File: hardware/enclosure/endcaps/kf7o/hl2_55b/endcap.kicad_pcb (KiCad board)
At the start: 2 copper layers, 106 x 55 mm, 14 parts, among them Q1 DTC144E, Q2 IRLML6402

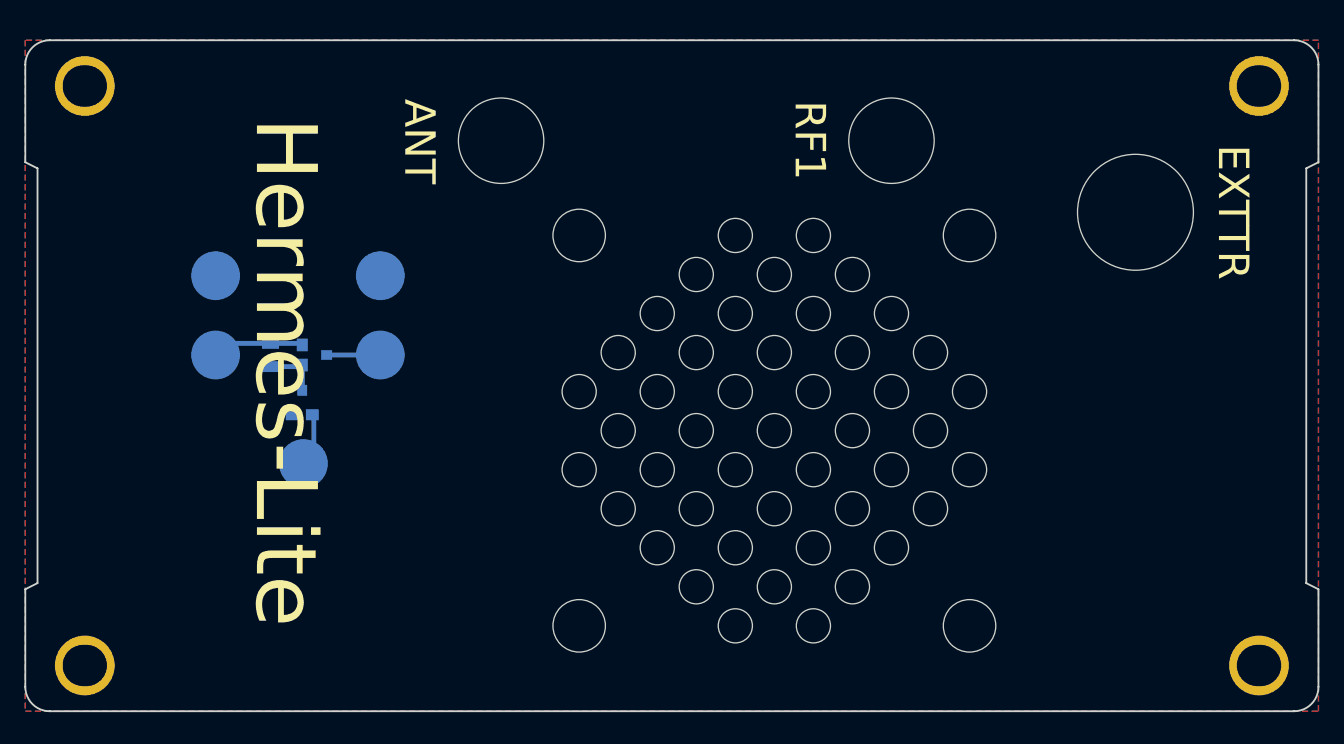
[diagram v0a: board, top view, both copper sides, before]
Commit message: 55mm rev2 endplate
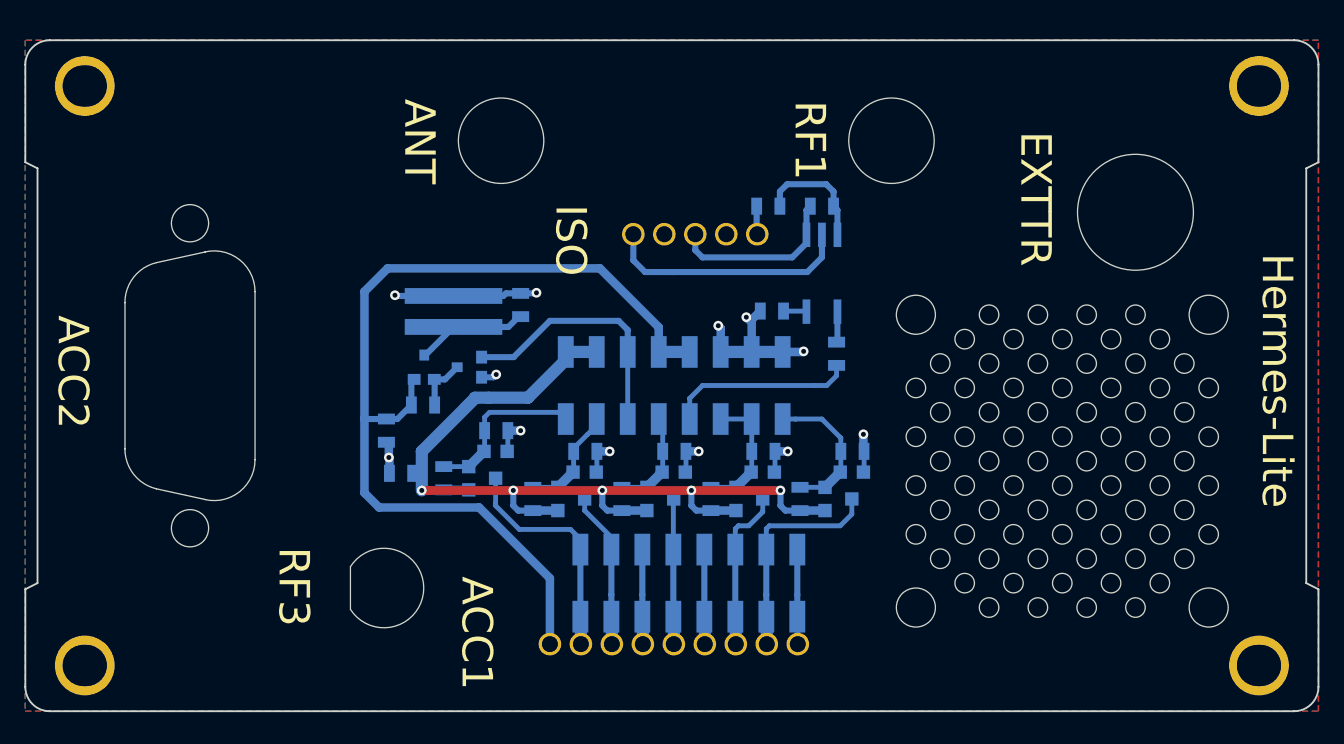
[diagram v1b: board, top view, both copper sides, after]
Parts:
- removed the REF** at (95.4, 66.0)
- removed TP1: Power, TestPoint:TestPoint_Pad_D4.0mm
- removed TP2: Fan Control, TestPoint:TestPoint_Pad_D4.0mm
- removed TP3, TP5: Ground, TestPoint:TestPoint_Pad_D4.0mm
- removed TP4: Fan Power, TestPoint:TestPoint_Pad_D4.0mm
- added ACC1: Terminal Block, endcaplib:terminal_block, B.Cu at (93.0, 99.5)
- added ACC2: DB9, endcaplib:db9inside, B.Cu at (63.5, 77.5)
- added C1: 0.1uF, endcaplib:SMD-0805, B.Cu at (115.3, 63.6)
- added C2: 0.1uF, endcaplib:SMD-0805, B.Cu at (79.6, 82.0)
- added C3: 0.1uF, endcaplib:SMD-0805, B.Cu at (80.8, 85.5)
- added C4: 0.1uF, endcaplib:SMD-0805, B.Cu at (90.6, 71.7)
- added FB1: Ferrite_Bead_Small, endcaplib:SMD-0805, B.Cu at (110.9, 63.6)
- added ISO1: Terminal Block, endcaplib:terminal_block5, B.Cu at (110.0, 65.9)
- added J2: Male Header, endcaplib:male_header, B.Cu at (94.3, 78.3)
- added J3: Male Header, endcaplib:male_header, B.Cu at (95.5, 94.5)
- added J4: Fan, endcaplib:male_header_2, B.Cu at (85.1, 73.5)
- added Q3: MULTIFET, endcaplib:3sot3_3, B.Cu at (89.5, 83.7)
- added Q4: MULTIFET, endcaplib:3sot3_3, B.Cu at (96.8, 85.4)
- added Q5: MULTIFET, endcaplib:3sot3_3, B.Cu at (104.1, 85.4)
- added Q6: MULTIFET, endcaplib:3sot3_3, B.Cu at (111.4, 85.4)
- added Q7: MULTIFET, endcaplib:3sot3_3, B.Cu at (118.7, 85.4)
- added R10: 10K, endcaplib:SMD-0805, B.Cu at (113.5, 87.6)
- added R11: 10K, endcaplib:SMD-0805, B.Cu at (117.8, 83.7)
- added R12: 1K, endcaplib:SMD-0805, B.Cu at (116.5, 75.7)
- added R13: 680, endcaplib:SMD-0805, B.Cu at (111.2, 72.2)
- added R2: 10K, endcaplib:SMD-0805, B.Cu at (84.3, 85.9)
- added R3: 10K, endcaplib:SMD-0805, B.Cu at (88.6, 82.0)
- added R4: 10K, endcaplib:SMD-0805, B.Cu at (91.6, 87.6)
- added R5: 10K, endcaplib:SMD-0805, B.Cu at (95.9, 83.7)
- added R6: 10K, endcaplib:SMD-0805, B.Cu at (98.9, 87.6)
- added R7: 10K, endcaplib:SMD-0805, B.Cu at (103.2, 83.7)
- added R8: 10K, endcaplib:SMD-0805, B.Cu at (106.2, 87.6)
- added R9: 10K, endcaplib:SMD-0805, B.Cu at (110.5, 83.7)
- added REF**: fan30, endcaplib:fan30, B.Cu at (123.0, 72.5)
- added RF3: SMA, endcaplib:sma_panel, B.Cu at (79.4, 94.9)
- added U1: ACPL-M21L-000E, Package_SO:SO-5_4.4x3.6mm_P1.27mm, B.Cu at (115.3, 69.1)
- moved Q1 15.2 mm to (87.4, 76.8), turned to 270 degrees
- moved R1 13.2 mm to (82.6, 79.9), turned to 0 degrees
- moved Q2 10.2 mm to (82.7, 77.8), turned to 180 degrees
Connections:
- net Earth renamed GNDS
- net Net-(Q2-Pad2) renamed VSUP
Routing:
- net Vlvds: track 0.00 -> 76.6 mm, vias 0 -> 5
- net VSUP: track 7.50 -> 78.0 mm
- net GNDS: track 0.00 -> 50.9 mm, vias 0 -> 12
- net Net-(ISO1-Pad5): track 0.00 -> 20.5 mm
- net Net-(ACC1-Pad2): track 0.00 -> 19.0 mm
- net Net-(ACC1-Pad8): track 0.00 -> 18.2 mm
- net Net-(J2-Pad5): track 4.35 -> 21.5 mm
- net ISOIN: track 0.00 -> 15.4 mm
- net Net-(J2-Pad2): track 0.00 -> 14.9 mm
- net Net-(C1-Pad2): track 0.00 -> 14.3 mm
- net Net-(J2-Pad16): track 0.00 -> 14.2 mm
- net Net-(ACC1-Pad7): track 0.00 -> 13.3 mm
- net Net-(ACC1-Pad3): track 0.00 -> 12.8 mm
- net Net-(ACC1-Pad5): track 0.00 -> 11.9 mm
- net Net-(J2-Pad12): track 0.00 -> 11.9 mm
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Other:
- board text added: "ACC1"
- board text added: "ACC2"
- board text added: "ISO"
- board text added: "RF3"

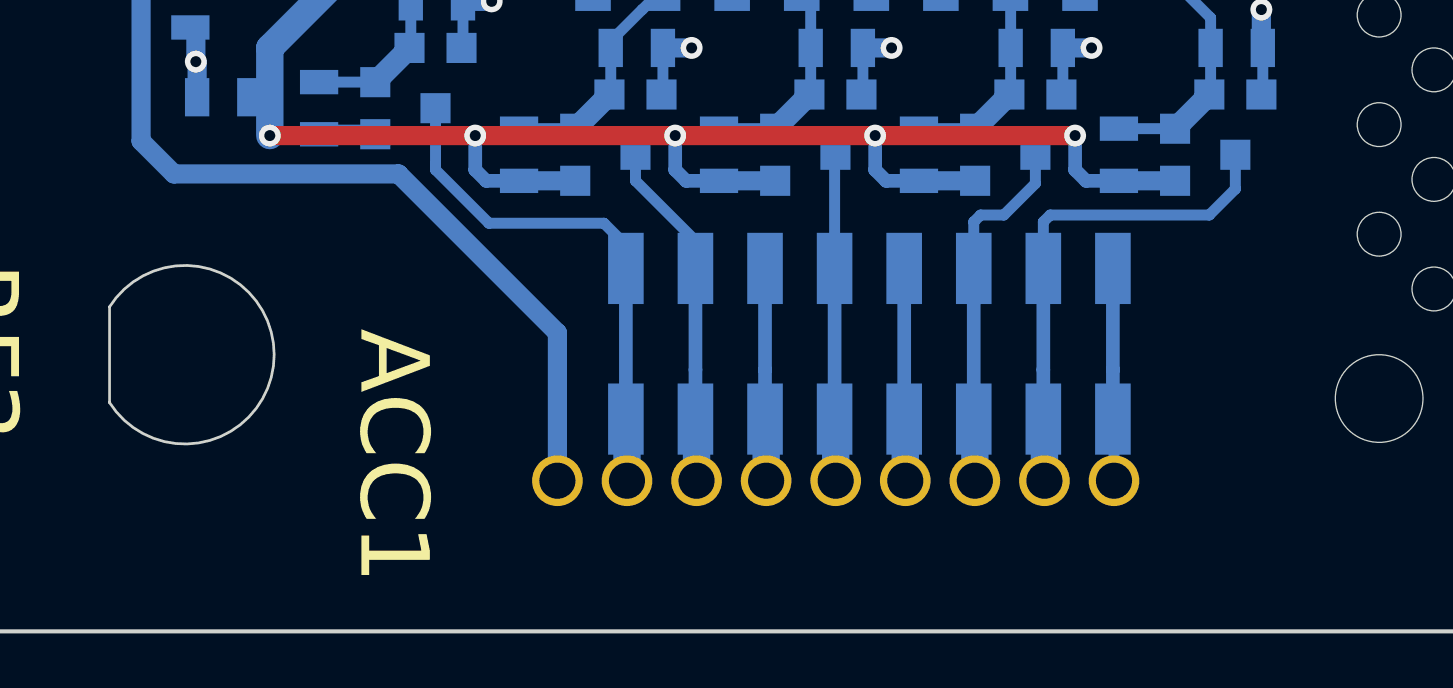
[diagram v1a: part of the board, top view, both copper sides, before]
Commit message: Added pullups, diodes to some channels
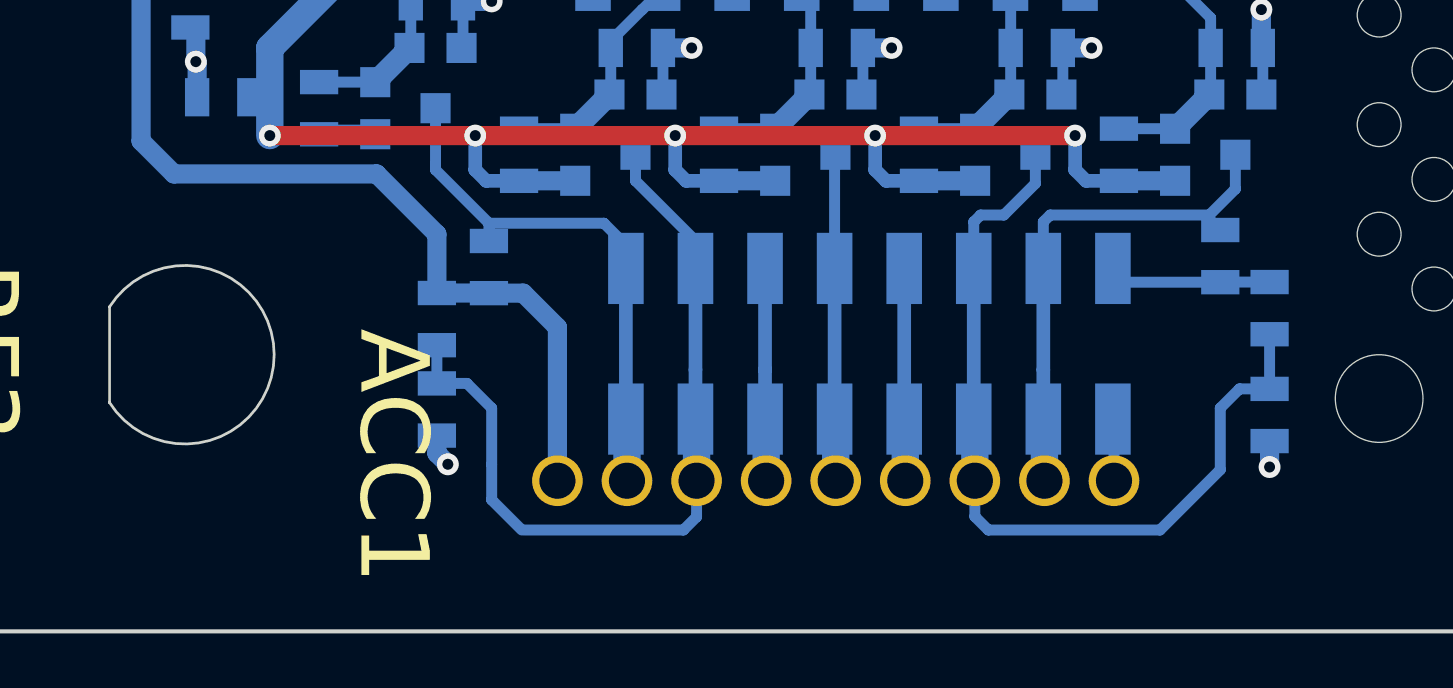
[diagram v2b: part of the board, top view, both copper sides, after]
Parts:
- added D1: 1N4148, endcaplib:SMD-0805, B.Cu at (119.0, 97.1)
- added D2: 1N4148, endcaplib:SMD-0805, B.Cu at (88.6, 96.9)
- added R14: 10K, endcaplib:SMD-0805, B.Cu at (117.2, 91.3)
- added R15: 10K, endcaplib:SMD-0805, B.Cu at (119.0, 93.2)
- added R16: 10K, endcaplib:SMD-0805, B.Cu at (88.6, 93.6)
- added R17: 10K, endcaplib:SMD-0805, B.Cu at (90.5, 91.7)
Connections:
- J3 pad 15: GNDS -> Net-(J3-Pad15)
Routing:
- net Net-(ACC1-Pad7): track 13.3 -> 31.1 mm
- net Net-(ACC1-Pad3): track 12.8 -> 29.3 mm
- net Net-(J3-Pad15): track 0.00 -> 5.93 mm
- net GNDS: track 50.9 -> 47.5 mm, vias 12 -> 14
- net VSUP: track 78.0 -> 79.4 mm
- net Net-(ACC1-Pad8): track 18.2 -> 18.9 mm
- net Net-(ACC1-Pad2): track 19.0 -> 19.6 mm

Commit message: Final IO end plates
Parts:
- added G***: OSHW-logo_silkscreen-back_2mm, HERMESLITE:OSHW-logo_silkscreen-back_2mm, B.Cu at (126.3, 53.6)
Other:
- board text added: "HL2 IO End Plate v2.0 © 2019 SofterHardware"
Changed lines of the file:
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@@
   (general
     (thickness 1.6)
-    (drawings 32)
+    (drawings 33)
     (tracks 288)
     (zones 0)
-    (modules 45)
+    (modules 46)
     (nets 29)
   )
@@
   (title_block
     (title "Hermes-Lite End Plate 55")
-    (date 2019-11-24)
+    (date 2019-12-01)
     (rev 2.0)
     (company SofterHardware)
@@
   )
   (setup
-    (last_trace_width 0.4)
+    (last_trace_width 0.25)
     (user_trace_width 0.2)
     (user_trace_width 0.4)
@@
     )
   )
+  (module HERMESLITE:OSHW-logo_silkscreen-back_2mm (layer B.Cu)
+    (at 126.3 53.6 180)
+    (fp_text reference G*** (at 0 -1.05918 180) (layer B.SilkS) hide
+      (effects (font (size 0.0889 0.0889) (thickness 0.01778)) (justify mirror))
+    )
+    (fp_text value OSHW-logo_silkscreen-back_2mm (at 0 1.05918 180) (layer B.SilkS) hide
+      (effects (font (size 0.0889 0.0889) (thickness 0.01778)) (justify mirror))
+    )
+    (fp_poly (pts (xy 0.60452 -0.89662) (xy 0.59436 -0.89154) (xy 0.5715 -0.8763) (xy 0.53848 -0.85598)
+      (xy 0.49784 -0.82804) (xy 0.45974 -0.80264) (xy 0.42672 -0.77978) (xy 0.40386 -0.76454)
+      (xy 0.3937 -0.75946) (xy 0.38862 -0.762) (xy 0.37084 -0.77216) (xy 0.3429 -0.78486)
+      (xy 0.32766 -0.79248) (xy 0.30226 -0.80518) (xy 0.28956 -0.80772) (xy 0.28702 -0.80264)
+      (xy 0.27686 -0.78486) (xy 0.26416 -0.75184) (xy 0.24384 -0.70866) (xy 0.22352 -0.65786)
+      (xy 0.20066 -0.60198) (xy 0.1778 -0.5461) (xy 0.15494 -0.49276) (xy 0.13462 -0.4445)
+      (xy 0.11938 -0.4064) (xy 0.10922 -0.37846) (xy 0.10414 -0.3683) (xy 0.10668 -0.36576)
+      (xy 0.11938 -0.35306) (xy 0.1397 -0.33782) (xy 0.18796 -0.29718) (xy 0.23368 -0.23876)
+      (xy 0.26416 -0.17272) (xy 0.27178 -0.09906) (xy 0.26416 -0.03302) (xy 0.23876 0.03048)
+      (xy 0.19304 0.09144) (xy 0.13716 0.13462) (xy 0.07112 0.16256) (xy 0 0.17018)
+      (xy -0.06858 0.16256) (xy -0.13462 0.13716) (xy -0.19558 0.09144) (xy -0.21844 0.0635)
+      (xy -0.254 0.00254) (xy -0.27432 -0.05842) (xy -0.27432 -0.07366) (xy -0.27178 -0.14478)
+      (xy -0.25146 -0.21336) (xy -0.2159 -0.27178) (xy -0.16256 -0.32258) (xy -0.15748 -0.32766)
+      (xy -0.13208 -0.34544) (xy -0.11684 -0.3556) (xy -0.10414 -0.36576) (xy -0.19304 -0.58166)
+      (xy -0.20828 -0.61722) (xy -0.23368 -0.67564) (xy -0.254 -0.72644) (xy -0.27178 -0.76708)
+      (xy -0.28448 -0.79248) (xy -0.28956 -0.80518) (xy -0.29718 -0.80518) (xy -0.31242 -0.8001)
+      (xy -0.3429 -0.78486) (xy -0.36322 -0.7747) (xy -0.38608 -0.76454) (xy -0.39624 -0.75946)
+      (xy -0.4064 -0.76454) (xy -0.42672 -0.77978) (xy -0.45974 -0.8001) (xy -0.49784 -0.8255)
+      (xy -0.5334 -0.8509) (xy -0.56896 -0.87376) (xy -0.59182 -0.889) (xy -0.60452 -0.89662)
+      (xy -0.60706 -0.89662) (xy -0.61722 -0.889) (xy -0.63754 -0.87376) (xy -0.66548 -0.84582)
+      (xy -0.70612 -0.80518) (xy -0.71374 -0.8001) (xy -0.74676 -0.76454) (xy -0.7747 -0.73406)
+      (xy -0.79502 -0.71374) (xy -0.8001 -0.70612) (xy -0.79502 -0.69342) (xy -0.77978 -0.66802)
+      (xy -0.75692 -0.635) (xy -0.72898 -0.59436) (xy -0.65786 -0.49022) (xy -0.6985 -0.3937)
+      (xy -0.70866 -0.36322) (xy -0.7239 -0.32766) (xy -0.7366 -0.30226) (xy -0.74168 -0.28956)
+      (xy -0.75184 -0.28702) (xy -0.77978 -0.2794) (xy -0.81788 -0.27178) (xy -0.8636 -0.26416)
+      (xy -0.90932 -0.254) (xy -0.94742 -0.24638) (xy -0.9779 -0.2413) (xy -0.9906 -0.23876)
+      (xy -0.99314 -0.23622) (xy -0.99568 -0.23114) (xy -0.99822 -0.21844) (xy -0.99822 -0.19304)
+      (xy -0.99822 -0.15494) (xy -0.99822 -0.09906) (xy -0.99822 -0.09398) (xy -0.99822 -0.04064)
+      (xy -0.99822 0) (xy -0.99568 0.0254) (xy -0.99314 0.03556) (xy -0.98044 0.04064)
+      (xy -0.9525 0.04572) (xy -0.9144 0.05334) (xy -0.86614 0.0635) (xy -0.8636 0.0635)
+      (xy -0.81534 0.07112) (xy -0.77724 0.08128) (xy -0.7493 0.08636) (xy -0.7366 0.09144)
+      (xy -0.73406 0.09398) (xy -0.7239 0.11176) (xy -0.7112 0.14224) (xy -0.69596 0.1778)
+      (xy -0.68072 0.21336) (xy -0.66548 0.24892) (xy -0.65786 0.27178) (xy -0.65532 0.28448)
+      (xy -0.66294 0.29464) (xy -0.67818 0.32004) (xy -0.70104 0.35306) (xy -0.72898 0.3937)
+      (xy -0.73152 0.39878) (xy -0.75946 0.43688) (xy -0.77978 0.47244) (xy -0.79502 0.4953)
+      (xy -0.8001 0.50546) (xy -0.8001 0.508) (xy -0.79248 0.51816) (xy -0.77216 0.54102)
+      (xy -0.74168 0.5715) (xy -0.70612 0.60706) (xy -0.69596 0.61722) (xy -0.65786 0.65532)
+      (xy -0.62992 0.68072) (xy -0.61214 0.69342) (xy -0.60452 0.6985) (xy -0.60452 0.69596)
+      (xy -0.59182 0.69088) (xy -0.56642 0.6731) (xy -0.5334 0.65024) (xy -0.49276 0.6223)
+      (xy -0.49022 0.61976) (xy -0.44958 0.59436) (xy -0.41656 0.5715) (xy -0.3937 0.55626)
+      (xy -0.38354 0.54864) (xy -0.381 0.54864) (xy -0.36576 0.55372) (xy -0.33528 0.56388)
+      (xy -0.30226 0.57658) (xy -0.26416 0.59182) (xy -0.23114 0.60706) (xy -0.20574 0.61722)
+      (xy -0.19304 0.62484) (xy -0.18796 0.64008) (xy -0.18288 0.67056) (xy -0.17272 0.7112)
+      (xy -0.1651 0.75946) (xy -0.16256 0.76708) (xy -0.15494 0.81534) (xy -0.14732 0.85344)
+      (xy -0.1397 0.88138) (xy -0.13716 0.89408) (xy -0.13208 0.89408) (xy -0.10668 0.89662)
+      (xy -0.07112 0.89662) (xy -0.02794 0.89662) (xy 0.01524 0.89662) (xy 0.05842 0.89662)
+      (xy 0.09652 0.89408) (xy 0.12192 0.89408) (xy 0.13462 0.89154) (xy 0.13462 0.889)
+      (xy 0.1397 0.8763) (xy 0.14478 0.84582) (xy 0.15494 0.80518) (xy 0.16256 0.75438)
+      (xy 0.1651 0.74676) (xy 0.17272 0.6985) (xy 0.18288 0.6604) (xy 0.18796 0.63246)
+      (xy 0.1905 0.6223) (xy 0.19558 0.61976) (xy 0.21336 0.61214) (xy 0.24638 0.59944)
+      (xy 0.28702 0.58166) (xy 0.37846 0.5461) (xy 0.49022 0.6223) (xy 0.50038 0.62992)
+      (xy 0.54102 0.65786) (xy 0.57404 0.67818) (xy 0.5969 0.69342) (xy 0.60706 0.6985)
+      (xy 0.61722 0.68834) (xy 0.64008 0.66802) (xy 0.67056 0.63754) (xy 0.70612 0.60452)
+      (xy 0.73152 0.57658) (xy 0.762 0.5461) (xy 0.78232 0.52578) (xy 0.79248 0.51054)
+      (xy 0.79756 0.50292) (xy 0.79502 0.49784) (xy 0.78994 0.48514) (xy 0.77216 0.46228)
+      (xy 0.7493 0.42672) (xy 0.72136 0.38862) (xy 0.6985 0.35306) (xy 0.67564 0.3175)
+      (xy 0.6604 0.28956) (xy 0.65278 0.27686) (xy 0.65532 0.27178) (xy 0.66294 0.24892)
+      (xy 0.67564 0.2159) (xy 0.69342 0.17526) (xy 0.73152 0.08636) (xy 0.78994 0.0762)
+      (xy 0.8255 0.06858) (xy 0.8763 0.06096) (xy 0.92202 0.0508) (xy 0.99568 0.03556)
+      (xy 0.99822 -0.23114) (xy 0.98806 -0.23622) (xy 0.97536 -0.2413) (xy 0.94996 -0.24638)
+      (xy 0.90932 -0.254) (xy 0.8636 -0.26162) (xy 0.8255 -0.26924) (xy 0.78486 -0.27686)
+      (xy 0.75692 -0.28194) (xy 0.74422 -0.28448) (xy 0.74168 -0.28956) (xy 0.73152 -0.30988)
+      (xy 0.71628 -0.34036) (xy 0.70104 -0.37592) (xy 0.6858 -0.41402) (xy 0.6731 -0.44958)
+      (xy 0.66294 -0.47498) (xy 0.65786 -0.49022) (xy 0.66294 -0.50038) (xy 0.67818 -0.52324)
+      (xy 0.70104 -0.55626) (xy 0.72644 -0.59436) (xy 0.75438 -0.635) (xy 0.77724 -0.66802)
+      (xy 0.79248 -0.69342) (xy 0.8001 -0.70358) (xy 0.79502 -0.7112) (xy 0.77978 -0.72898)
+      (xy 0.75184 -0.75946) (xy 0.70612 -0.80518) (xy 0.6985 -0.81026) (xy 0.66548 -0.84582)
+      (xy 0.635 -0.87122) (xy 0.61468 -0.89154) (xy 0.60452 -0.89662)) (layer B.SilkS) (width 0.00254))
+  )
+  (gr_text "HL2 IO End Plate v2.0\n© 2019 SofterHardware" (at 146 53.7) (layer B.SilkS)
+    (effects (font (size 1 1) (thickness 0.12)) (justify left mirror))
+  )
   (gr_text ACC2 (at 63.6 58.2 180) (layer Eco1.User)
